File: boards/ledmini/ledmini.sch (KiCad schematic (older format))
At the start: 50 parts, among them IC1 ATMEGA168-M, IC2 SN75176B, SW1 SW_PUSH, U1 LM7805, X1 CRYSTAL

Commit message: finished ledmini, controller, and comm boards -- need to re-panelize myro boards
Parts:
- C1, C4: footprint C1 -> SM0402; DigikeyPart 478-5812-ND -> 445-1415-1-ND; Part TAP105M035SCS -> C1005X5R0J105M
- C10, C11: footprint SM0805 -> SM0402; DigikeyPart 311-1097-1-ND -> 445-4891-1-ND; Part CC0805DRNP09BN8R0 -> C1005C0G1H080D
- C2, C6: footprint C1 -> SM0402; DigikeyPart 478-4862-ND -> 445-3445-1-ND; Part SR215C103KAR -> C1005Y5V1E104Z
- C5: footprint C1 -> SM0402; DigikeyPart 478-1831-ND -> 445-3445-1-ND; Part TAP104K035SCS -> C1005Y5V1E104Z
- C7, C8: footprint C1 -> SM0402; DigikeyPart 478-4862-ND -> 445-1256-1-ND; Part SR215C103KAR -> C1005X7R1H102K
- C9: footprint SM0805 -> SM0402; DigikeyPart 08055C104KAT2A -> 445-3445-1-ND; Part 478-1395-1-ND -> C1005Y5V1E104Z
- IC1: footprint MLF/QFN32 -> TQFP32; DigikeyPart (none) -> ATMEGA168P-20AU-ND; Part (none) -> ATMEGA168P-20AU
- IC2: footprint DIP-8__300 -> SOIC8; DigikeyPart 296-1739-5-ND -> 296-1275-5-ND; Part SN75176BP -> SN75176BD
- R1, R6, R7, R8, R9: footprint SM0805 -> SM0402; DigikeyPart RMCF0805JT1K00CT-ND -> RMCF0402JT1K00CT-ND; Part RMCF0805JT1K00 -> RMCF0402JT1K00
- R10: footprint SM0805 -> SM0402; DigikeyPart RMCF0805JT120RCT-ND -> P120JCT-ND; Part RMCF0805JT120R -> ERJ-2GEJ121X
- R2: footprint SM0805 -> SM0402; DigikeyPart RMCF0805JT10K0CT-ND -> RMCF0402JT10K0CT-ND; Part RMCF0805JT10K0 -> RMCF0402JT10K0
- R3: footprint SM0805 -> SM0402; DigikeyPart RMCF0805JT330RCT-ND -> ERJ-2GEJ331X; Part RMCF0805JT330R -> P330JCT-ND
- TLC1: footprint DIP-28__300 -> SSOP28; DigikeyPart 296-17732-5-ND -> 296-17733-5-ND; Part TLC5940NT -> TLC5940PWP
- X1: footprint SM1206 -> Crystal_FOX-FE_SMD_RevA_09Aug2010
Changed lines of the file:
@@
-EESchema Schematic File Version 2  date Sun 17 Jul 2011 04:04:47 PM EDT
+EESchema Schematic File Version 2  date Sun 07 Aug 2011 06:13:35 PM EDT
 LIBS:power
 LIBS:device
@@
 LIBS:SparkFun
 LIBS:ledmini-cache
-EELAYER 24  0
+EELAYER 25  0
 EELAYER END
 $Descr A 11000 8500
+encoding utf-8
 Sheet 1 1
 Title "Mini LED Controller Board"
-Date "17 jul 2011"
+Date "7 aug 2011"
 Rev "1.5"
 Comp "J. Colosimo"
@@
 F 0 "IC1" H 3500 4900 50  0000 L BNN
 F 1 "ATMEGA168-M" H 4450 2250 50  0000 L BNN
-F 2 "MLF/QFN32" H 3750 2300 50  0001 C CNN
+F 2 "TQFP32" H 3750 2300 50  0001 C CNN
+F 4 "ATMEGA168P-20AU" H 4200 3650 60  0001 C CNN "Part"
+F 5 "ATMEGA168P-20AU-ND" H 4200 3650 60  0001 C CNN "DigikeyPart"
 	1    4200 3650
 	1    0    0    -1
@@
 F 0 "R3" V 7600 2400 50  0000 C CNN
 F 1 "325.5" V 7700 2400 50  0000 C CNN
-F 2 "SM0805" V 7550 2350 60  0001 C CNN
-F 4 "RMCF0805JT330R" H 7700 2400 60  0001 C CNN "Part"
-F 5 "RMCF0805JT330RCT-ND" H 7700 2400 60  0001 C CNN "DigikeyPart"
+F 2 "SM0402" V 7550 2350 60  0001 C CNN
+F 4 "P330JCT-ND" H 7700 2400 60  0001 C CNN "Part"
+F 5 "ERJ-2GEJ331X" H 7700 2400 60  0001 C CNN "DigikeyPart"
 	1    7700 2400
 	1    0    0    -1
@@
 F 0 "R10" V 2780 5850 50  0000 C CNN
 F 1 "120" V 2700 5850 50  0000 C CNN
-F 2 "SM0805" V 2830 5800 60  0001 C CNN
-F 4 "RMCF0805JT120R" H 2700 5850 60  0001 C CNN "Part"
-F 5 "RMCF0805JT120RCT-ND" H 2700 5850 60  0001 C CNN "DigikeyPart"
+F 2 "SM0402" V 2830 5800 60  0001 C CNN
+F 4 "ERJ-2GEJ121X" H 2700 5850 60  0001 C CNN "Part"
+F 5 "P120JCT-ND" H 2700 5850 60  0001 C CNN "DigikeyPart"
 	1    2700 5850
 	1    0    0    -1
@@
 F 0 "C8" H 2100 1700 50  0000 L CNN
 F 1 "1nF" H 2000 1500 50  0000 L CNN
-F 2 "C1" H 2050 1600 60  0001 C CNN
-F 4 "SR215C103KAR" H 2050 1600 60  0001 C CNN "Part"
-F 5 "478-4862-ND" H 2050 1600 60  0001 C CNN "DigikeyPart"
+F 2 "SM0402" H 2050 1600 60  0001 C CNN
+F 4 "C1005X7R1H102K" H 2050 1600 60  0001 C CNN "Part"
+F 5 "445-1256-1-ND" H 2050 1600 60  0001 C CNN "DigikeyPart"
 	1    2050 1600
 	-1   0    0    1
@@
 F 0 "R9" V 6430 3950 50  0000 C CNN
 F 1 "1K" V 6350 3950 50  0000 C CNN
-F 2 "SM0805" V 6480 3900 60  0001 C CNN
-F 4 "RMCF0805JT1K00" H 6350 3950 60  0001 C CNN "Part"
-F 5 "RMCF0805JT1K00CT-ND" H 6350 3950 60  0001 C CNN "DigikeyPart"
+F 2 "SM0402" V 6480 3900 60  0001 C CNN
+F 4 "RMCF0402JT1K00" H 6350 3950 60  0001 C CNN "Part"
+F 5 "RMCF0402JT1K00CT-ND" H 6350 3950 60  0001 C CNN "DigikeyPart"
 	1    6350 3950
 	0    1    1    0
@@
 F 0 "R8" V 6430 3750 50  0000 C CNN
 F 1 "1K" V 6350 3750 50  0000 C CNN
-F 2 "SM0805" V 6480 3700 60  0001 C CNN
-F 4 "RMCF0805JT1K00" H 6350 3750 60  0001 C CNN "Part"
-F 5 "RMCF0805JT1K00CT-ND" H 6350 3750 60  0001 C CNN "DigikeyPart"
+F 2 "SM0402" V 6480 3700 60  0001 C CNN
+F 4 "RMCF0402JT1K00" H 6350 3750 60  0001 C CNN "Part"
+F 5 "RMCF0402JT1K00CT-ND" H 6350 3750 60  0001 C CNN "DigikeyPart"
 	1    6350 3750
 	0    1    1    0
@@
 F 0 "R7" V 6430 3550 50  0000 C CNN
 F 1 "1K" V 6350 3550 50  0000 C CNN
-F 2 "SM0805" V 6480 3500 60  0001 C CNN
-F 4 "RMCF0805JT1K00" H 6350 3550 60  0001 C CNN "Part"
-F 5 "RMCF0805JT1K00CT-ND" H 6350 3550 60  0001 C CNN "DigikeyPart"
+F 2 "SM0402" V 6480 3500 60  0001 C CNN
+F 4 "RMCF0402JT1K00" H 6350 3550 60  0001 C CNN "Part"
+F 5 "RMCF0402JT1K00CT-ND" H 6350 3550 60  0001 C CNN "DigikeyPart"
 	1    6350 3550
 	0    1    1    0
@@
 F 0 "R6" V 6430 3350 50  0000 C CNN
 F 1 "1K" V 6350 3350 50  0000 C CNN
-F 2 "SM0805" V 6480 3300 60  0001 C CNN
-F 4 "RMCF0805JT1K00" H 6350 3350 60  0001 C CNN "Part"
-F 5 "RMCF0805JT1K00CT-ND" H 6350 3350 60  0001 C CNN "DigikeyPart"
+F 2 "SM0402" V 6480 3300 60  0001 C CNN
+F 4 "RMCF0402JT1K00" H 6350 3350 60  0001 C CNN "Part"
+F 5 "RMCF0402JT1K00CT-ND" H 6350 3350 60  0001 C CNN "DigikeyPart"
 	1    6350 3350
 	0    1    1    0
@@
 F 0 "C10" H 4400 1950 50  0000 L CNN
 F 1 "8pF" H 4400 1750 50  0000 L CNN
-F 2 "SM0805" H 4350 1850 60  0001 C CNN
-F 4 "CC0805DRNP09BN8R0" H 4350 1850 60  0001 C CNN "Part"
-F 5 "311-1097-1-ND" H 4350 1850 60  0001 C CNN "DigikeyPart"
+F 2 "SM0402" H 4350 1850 60  0001 C CNN
+F 4 "C1005C0G1H080D" H 4350 1850 60  0001 C CNN "Part"
+F 5 "445-4891-1-ND" H 4350 1850 60  0001 C CNN "DigikeyPart"
 	1    4350 1850
 	1    0    0    -1
@@
 F 0 "R1" V 3880 1150 50  0000 C CNN
 F 1 "1K" V 3800 1150 50  0000 C CNN
-F 2 "SM0805" V 3930 1100 60  0001 C CNN
-F 4 "RMCF0805JT1K00" H 3800 1150 60  0001 C CNN "Part"
-F 5 "RMCF0805JT1K00CT-ND" H 3800 1150 60  0001 C CNN "DigikeyPart"
+F 2 "SM0402" V 3930 1100 60  0001 C CNN
+F 4 "RMCF0402JT1K00" H 3800 1150 60  0001 C CNN "Part"
+F 5 "RMCF0402JT1K00CT-ND" H 3800 1150 60  0001 C CNN "DigikeyPart"
 	1    3800 1150
 	1    0    0    -1
@@
 F 0 "C5" H 1850 1700 50  0000 L CNN
 F 1 "100nF" H 1700 1500 50  0000 L CNN
-F 2 "C1" H 1800 1600 60  0001 C CNN
-F 4 "TAP104K035SCS" H 1800 1600 60  0001 C CNN "Part"
-F 5 "478-1831-ND" H 1800 1600 60  0001 C CNN "DigikeyPart"
+F 2 "SM0402" H 1800 1600 60  0001 C CNN
+F 4 "C1005Y5V1E104Z" H 1800 1600 60  0001 C CNN "Part"
+F 5 "445-3445-1-ND" H 1800 1600 60  0001 C CNN "DigikeyPart"
 	1    1800 1600
 	-1   0    0    1
@@
 F 0 "C6" H 2950 1300 50  0000 L CNN
 F 1 "100nF" H 2800 1100 50  0000 L CNN
-F 2 "C1" H 2900 1200 60  0001 C CNN
-F 4 "SR215C103KAR" H 2900 1200 60  0001 C CNN "Part"
-F 5 "478-4862-ND" H 2900 1200 60  0001 C CNN "DigikeyPart"
+F 2 "SM0402" H 2900 1200 60  0001 C CNN
+F 4 "C1005Y5V1E104Z" H 2900 1200 60  0001 C CNN "Part"
+F 5 "445-3445-1-ND" H 2900 1200 60  0001 C CNN "DigikeyPart"
 	1    2900 1200
 	1    0    0    -1
@@
 F 0 "C7" H 3200 1300 50  0000 L CNN
 F 1 "1nF" H 3100 1100 50  0000 L CNN
-F 2 "C1" H 3150 1200 60  0001 C CNN
-F 4 "SR215C103KAR" H 3150 1200 60  0001 C CNN "Part"
-F 5 "478-4862-ND" H 3150 1200 60  0001 C CNN "DigikeyPart"
+F 2 "SM0402" H 3150 1200 60  0001 C CNN
+F 4 "C1005X7R1H102K" H 3150 1200 60  0001 C CNN "Part"
+F 5 "445-1256-1-ND" H 3150 1200 60  0001 C CNN "DigikeyPart"
 	1    3150 1200
 	1    0    0    -1
@@
 F 0 "C4" H 1600 1700 50  0000 L CNN
 F 1 "1uF" H 1500 1500 50  0000 L CNN
-F 2 "C1" H 1550 1600 60  0001 C CNN
-F 4 "TAP105M035SCS" H 1550 1600 60  0001 C CNN "Part"
-F 5 "478-5812-ND" H 1550 1600 60  0001 C CNN "DigikeyPart"
+F 2 "SM0402" H 1550 1600 60  0001 C CNN
+F 4 "C1005X5R0J105M" H 1550 1600 60  0001 C CNN "Part"
+F 5 "445-1415-1-ND" H 1550 1600 60  0001 C CNN "DigikeyPart"
 	1    1550 1600
 	-1   0    0    1
@@
 F 0 "C2" H 1700 1300 50  0000 L CNN
 F 1 "100nF" H 1550 1100 50  0000 L CNN
-F 2 "C1" H 1650 1200 60  0001 C CNN
-F 4 "SR215C103KAR" H 1650 1200 60  0001 C CNN "Part"
-F 5 "478-4862-ND" H 1650 1200 60  0001 C CNN "DigikeyPart"
+F 2 "SM0402" H 1650 1200 60  0001 C CNN
+F 4 "C1005Y5V1E104Z" H 1650 1200 60  0001 C CNN "Part"
+F 5 "445-3445-1-ND" H 1650 1200 60  0001 C CNN "DigikeyPart"
 	1    1650 1200
 	1    0    0    -1
@@
 F 0 "C1" H 1450 1300 50  0000 L CNN
 F 1 "1uF" H 1350 1100 50  0000 L CNN
-F 2 "C1" H 1400 1200 60  0001 C CNN
-F 4 "TAP105M035SCS" H 1400 1200 60  0001 C CNN "Part"
-F 5 "478-5812-ND" H 1400 1200 60  0001 C CNN "DigikeyPart"
+F 2 "SM0402" H 1400 1200 60  0001 C CNN
+F 4 "C1005X5R0J105M" H 1400 1200 60  0001 C CNN "Part"
+F 5 "445-1415-1-ND" H 1400 1200 60  0001 C CNN "DigikeyPart"
 	1    1400 1200
 	1    0    0    -1
@@
 F 0 "C9" V 6250 5250 50  0000 L CNN
 F 1 "100nF" V 6250 5000 50  0000 L CNN
-F 2 "SM0805" H 6200 5150 60  0001 C CNN
-F 4 "478-1395-1-ND" H 6200 5150 60  0001 C CNN "Part"
-F 5 "08055C104KAT2A" H 6200 5150 60  0001 C CNN "DigikeyPart"
+F 2 "SM0402" H 6200 5150 60  0001 C CNN
+F 4 "C1005Y5V1E104Z" H 6200 5150 60  0001 C CNN "Part"
+F 5 "445-3445-1-ND" H 6200 5150 60  0001 C CNN "DigikeyPart"
 	1    6200 5150
 	0    1    1    0
@@
 F 0 "R2" V 6180 4700 50  0000 C CNN
 F 1 "10K" V 6100 4700 50  0000 C CNN
-F 2 "SM0805" V 6230 4650 60  0001 C CNN
-F 4 "RMCF0805JT10K0" H 6100 4700 60  0001 C CNN "Part"
-F 5 "RMCF0805JT10K0CT-ND" H 6100 4700 60  0001 C CNN "DigikeyPart"
+F 2 "SM0402" V 6230 4650 60  0001 C CNN
+F 4 "RMCF0402JT10K0" H 6100 4700 60  0001 C CNN "Part"
+F 5 "RMCF0402JT10K0CT-ND" H 6100 4700 60  0001 C CNN "DigikeyPart"
 	1    6100 4700
 	0    -1   -1   0
@@
 F 0 "C11" H 5000 1950 50  0000 L CNN
 F 1 "8pF" H 5000 1750 50  0000 L CNN
-F 2 "SM0805" H 4950 1850 60  0001 C CNN
-F 4 "CC0805DRNP09BN8R0" H 4950 1850 60  0001 C CNN "Part"
-F 5 "311-1097-1-ND" H 4950 1850 60  0001 C CNN "DigikeyPart"
+F 2 "SM0402" H 4950 1850 60  0001 C CNN
+F 4 "C1005C0G1H080D" H 4950 1850 60  0001 C CNN "Part"
+F 5 "445-4891-1-ND" H 4950 1850 60  0001 C CNN "DigikeyPart"
 	1    4950 1850
 	1    0    0    -1
@@
 F 0 "X1" H 4650 2300 60  0000 C CNN
 F 1 "CRYSTAL" H 4650 2000 60  0000 C CNN
-F 2 "SM1206" H 4590 2360 60  0001 C CNN
+F 2 "Crystal_FOX-FE_SMD_RevA_09Aug2010" H 4590 2360 60  0001 C CNN
 F 4 "NX8045GB-20.000000MHZ" H 4650 2150 60  0001 C CNN "Part"
 F 5 "644-1026-1-ND" H 4650 2150 60  0001 C CNN "DigikeyPart"
@@
 F 0 "TLC1" H 8500 1550 60  0000 C CNN
 F 1 "TLC5940" H 8500 1650 60  0000 C CNN
-F 2 "DIP-28__300" H 8500 1650 60  0001 C CNN
-F 4 "TLC5940NT" H 8500 1650 60  0001 C CNN "Part"
-F 5 "296-17732-5-ND" H 8500 1650 60  0001 C CNN "DigikeyPart"
+F 2 "SSOP28" H 8500 1650 60  0001 C CNN
+F 4 "TLC5940PWP" H 8500 1650 60  0001 C CNN "Part"
+F 5 "296-17733-5-ND" H 8500 1650 60  0001 C CNN "DigikeyPart"
 	1    8500 1650
 	-1   0    0    -1
@@
 F 0 "IC2" H 2440 6470 50  0000 L BNN
 F 1 "SN75176B" H 2440 5560 50  0000 L BNN
-F 2 "DIP-8__300" H 2800 6050 50  0001 C CNN
-F 4 "SN75176BP" H 3150 5950 60  0001 C CNN "Part"
-F 5 "296-1739-5-ND" H 3150 5950 60  0001 C CNN "DigikeyPart"
+F 2 "SOIC8" H 2800 6050 50  0001 C CNN
+F 4 "SN75176BD" H 3150 5950 60  0001 C CNN "Part"
+F 5 "296-1275-5-ND" H 3150 5950 60  0001 C CNN "DigikeyPart"
 	1    3150 5950
 	-1   0    0    -1

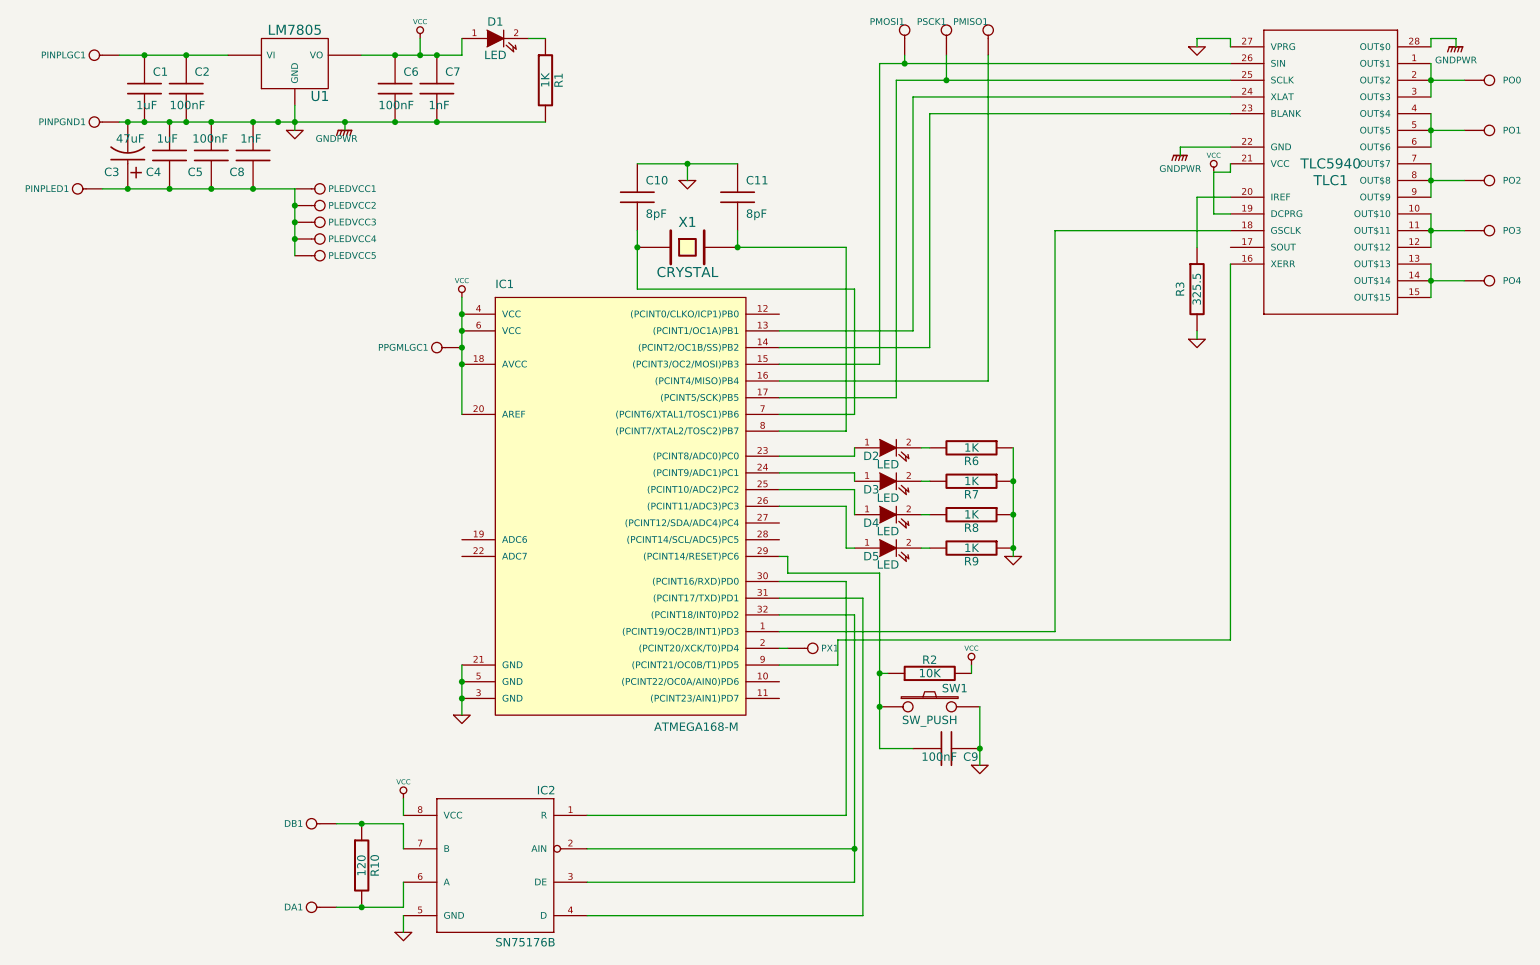
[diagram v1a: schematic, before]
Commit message: Revision 1.6 of boards ready (silkscreen fixes), modified package script to convert SVG->PNG automatically (SVG->PDF doesn't work D:).
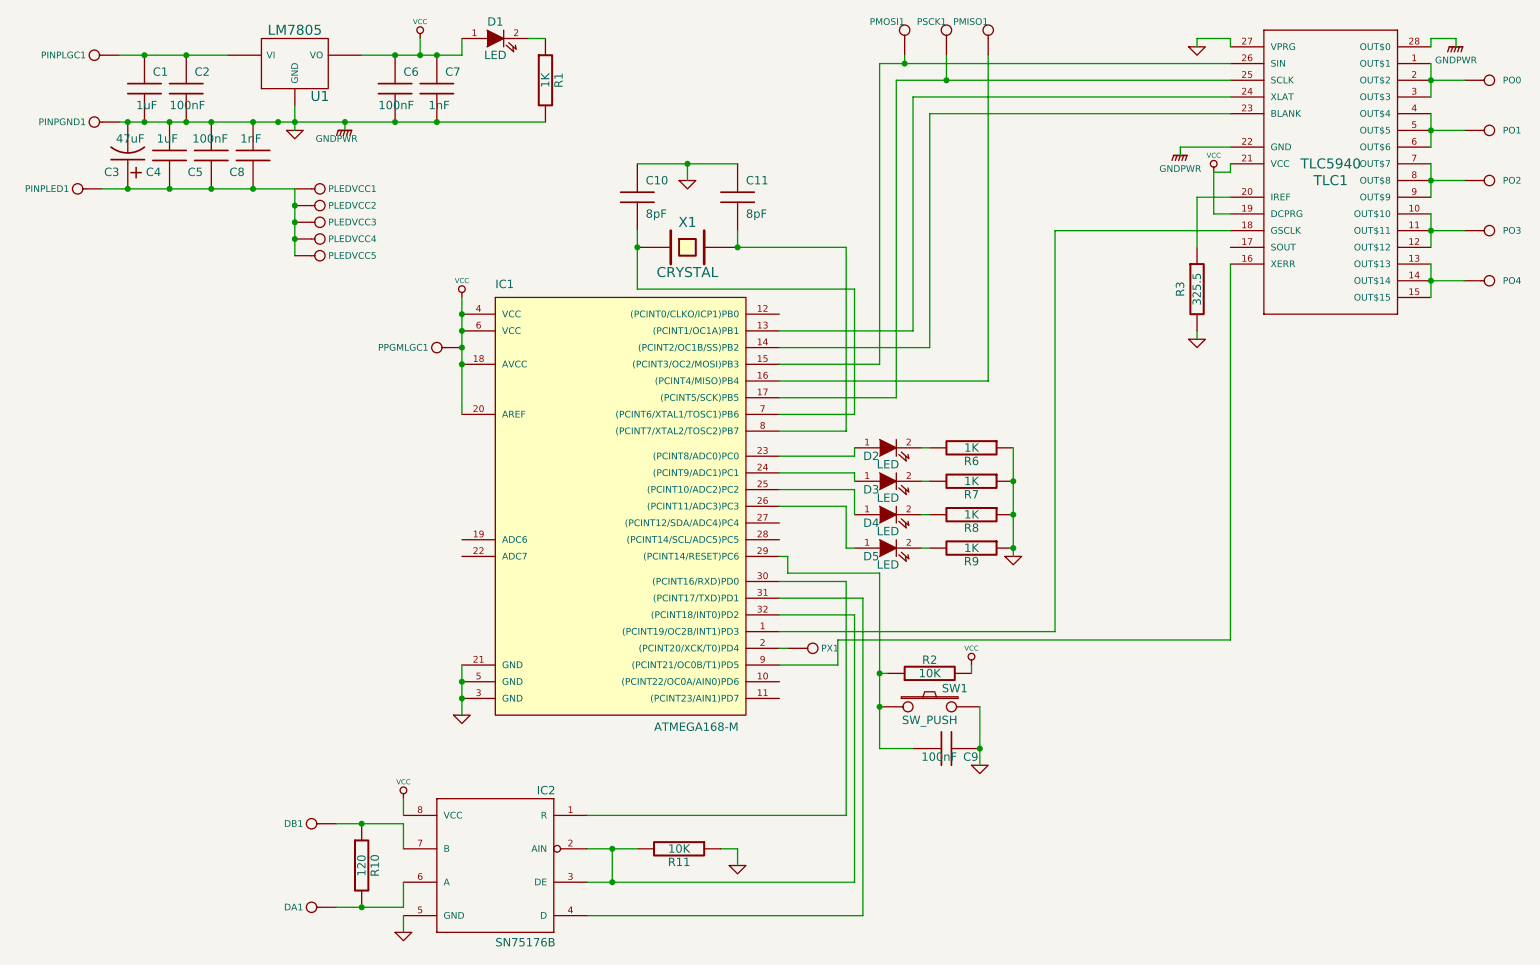
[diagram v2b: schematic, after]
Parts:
- added R11: 10K, symbol R
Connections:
- net GND: now also R11.1
- net at IC1.32 ((PCINT18/INT0)PD2), IC2.2 (AIN), IC2.3 (DE): now also R11.2
